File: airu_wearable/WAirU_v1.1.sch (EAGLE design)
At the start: 57 parts, among them J2 2p-2.0, Q2 MMBT3904LT1G, Q3 MMBT3904LT1G, Q4 BSS84, Q6 BSS84, U2 CN3065-DFN8, U3 HDC1080DMBT, U4 CJT1117-3.3-SOT223, U6 PAM2401, U7 ESP32_WROOM32_SKINNY

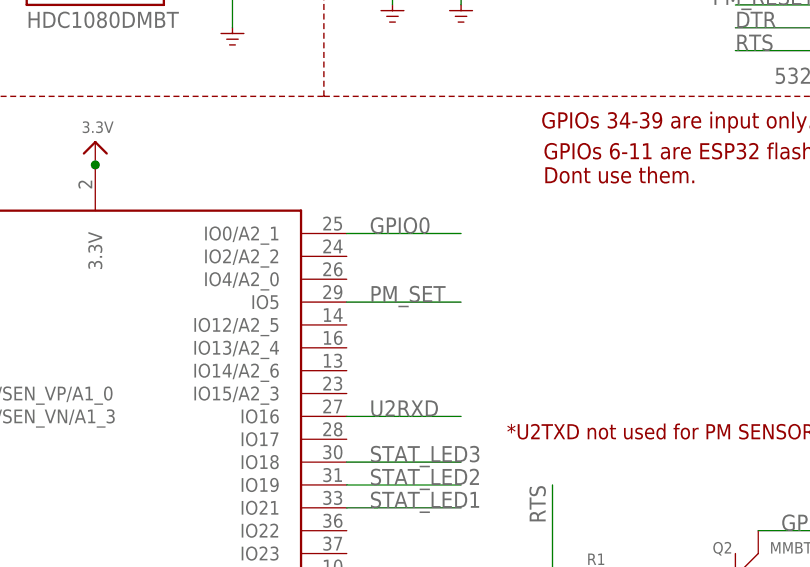
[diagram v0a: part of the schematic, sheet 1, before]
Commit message: changed PM_SET to GPIO4
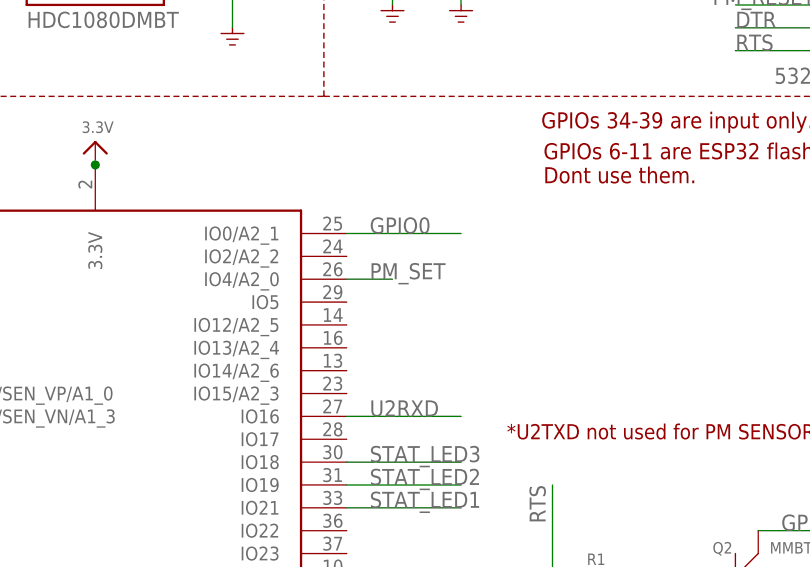
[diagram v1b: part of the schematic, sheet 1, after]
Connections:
- net PM_SET: now also U7.IO4/A2_0; no longer U7.IO5
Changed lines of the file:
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@@
 <net name="PM_SET" class="0">
-<segment>
-<pinref part="U7" gate="G$1" pin="IO5"/>
-<wire x1="78.74" y1="109.22" x2="91.44" y2="109.22" width="0.1524" layer="91"/>
-<label x="81.28" y="109.22" size="1.778" layer="95"/>
-</segment>
 <segment>
 <wire x1="121.92" y1="149.86" x2="134.62" y2="149.86" width="0.1524" layer="91"/>
@@
 <pinref part="U7" gate="G$1" pin="RXD0"/>
 </segment>
+<segment>
+<pinref part="U7" gate="G$1" pin="IO4/A2_0"/>
+<wire x1="78.74" y1="111.76" x2="83.82" y2="111.76" width="0.1524" layer="91"/>
+<label x="81.28" y="111.76" size="1.778" layer="95"/>
+</segment>
 </net>

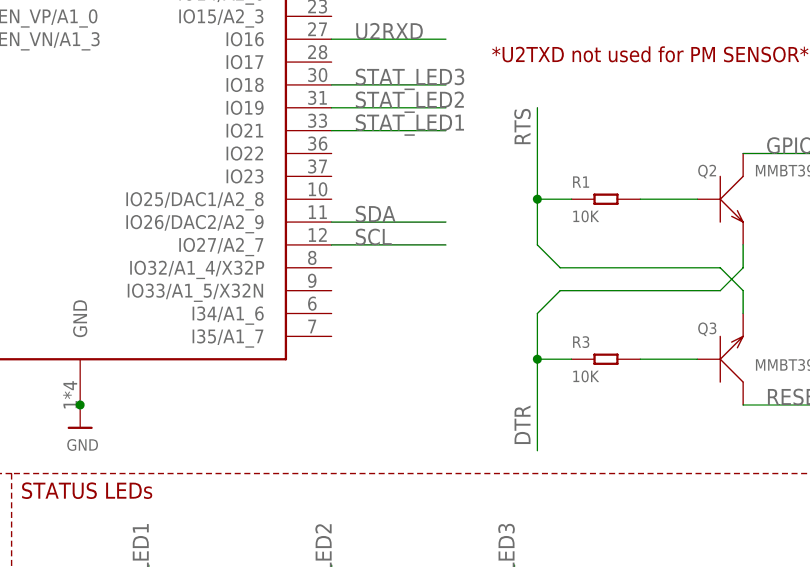
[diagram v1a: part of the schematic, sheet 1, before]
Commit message: routed PM_RESET and added dimensions, removed GND polygon from upper left
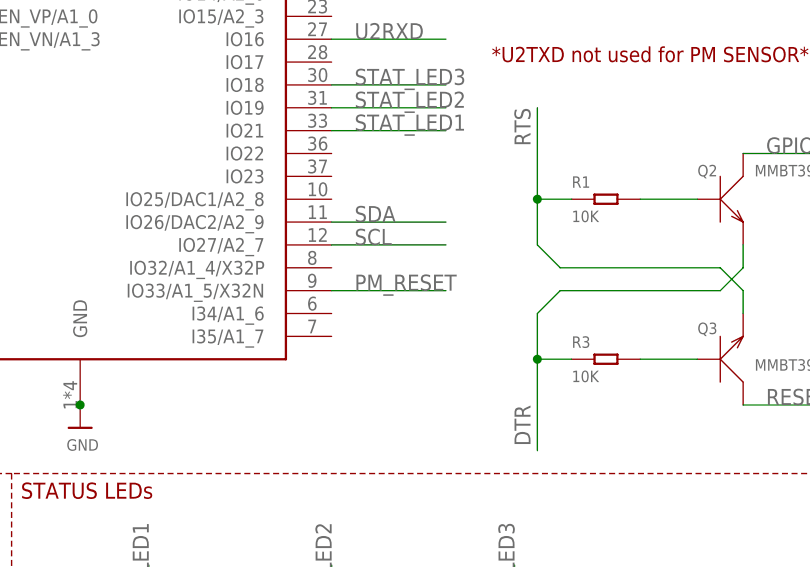
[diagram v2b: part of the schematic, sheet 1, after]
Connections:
- net PM_RESET: now also U7.IO33/A1_5/X32N
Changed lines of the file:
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@@
 <label x="119.38" y="142.24" size="1.778" layer="95"/>
+</segment>
+<segment>
+<pinref part="U7" gate="G$1" pin="IO33/A1_5/X32N"/>
+<wire x1="78.74" y1="68.58" x2="91.44" y2="68.58" width="0.1524" layer="91"/>
+<label x="81.28" y="68.58" size="1.778" layer="95"/>
 </segment>
 </net>

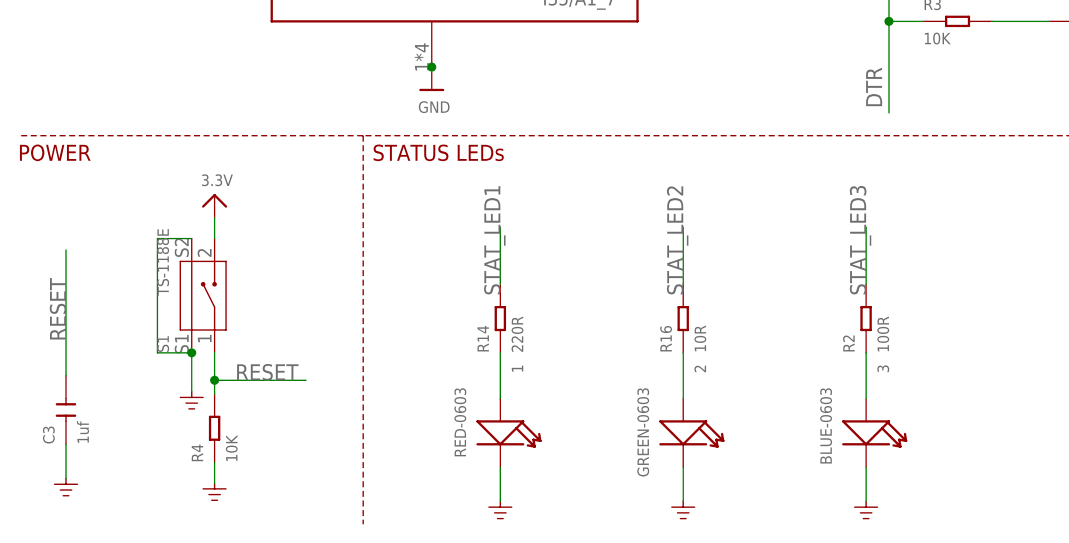
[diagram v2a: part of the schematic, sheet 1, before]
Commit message: - Remove led - Re-position Status Led 1 near the button - Replace reset button with SMD one - Route GND signal to ground plan - Add heat dissipation surrounding the temperature sensor - Remove ground plane copper pour from temperature sensor - Adjust board dimension, mounting holes dimention and position
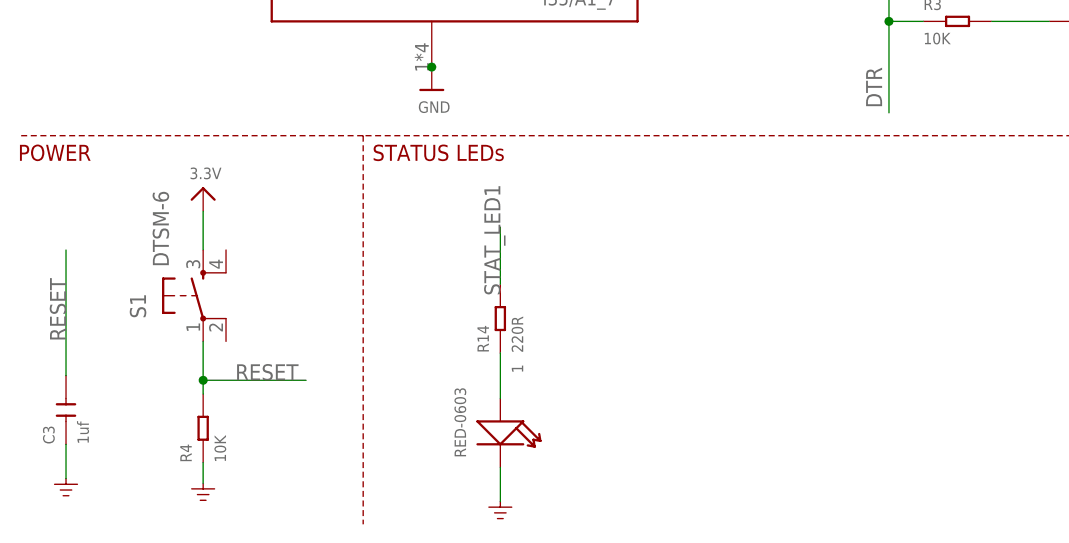
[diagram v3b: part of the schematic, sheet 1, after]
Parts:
- removed 2: GREEN-0603, Seeed-LED:SMD-LED-CLEAR-GREEN(0603)
- removed 3: BLUE-0603, Seeed-LED:SMD-LED-CLEAR-BLUE(0603)
- removed R16: 10R, Seeed-Resistor:SMD-RES-10R-5%-1/10W(0603)
- removed R2: 100R, Seeed-Resistor:SMD-RES-100R-5%-1/10W(0603)
- S1: value TS-1188E -> DTSM-6; device OPL_Switch:SMD-BUTTON(2+2P-7X3.5MM-90D) -> switch-tact:DTSM-6
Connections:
- removed net N$1: 2.+, R16.1
- removed net N$22: 3.+, R2.1
- net 3.3V: now also S1.3; no longer S1.2
- net GND: no longer 2.-, 3.-, S1.S1, S1.S2
- net STAT_LED2: no longer R16.2
- net STAT_LED3: no longer R2.2
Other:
- moved on the sheet: R4

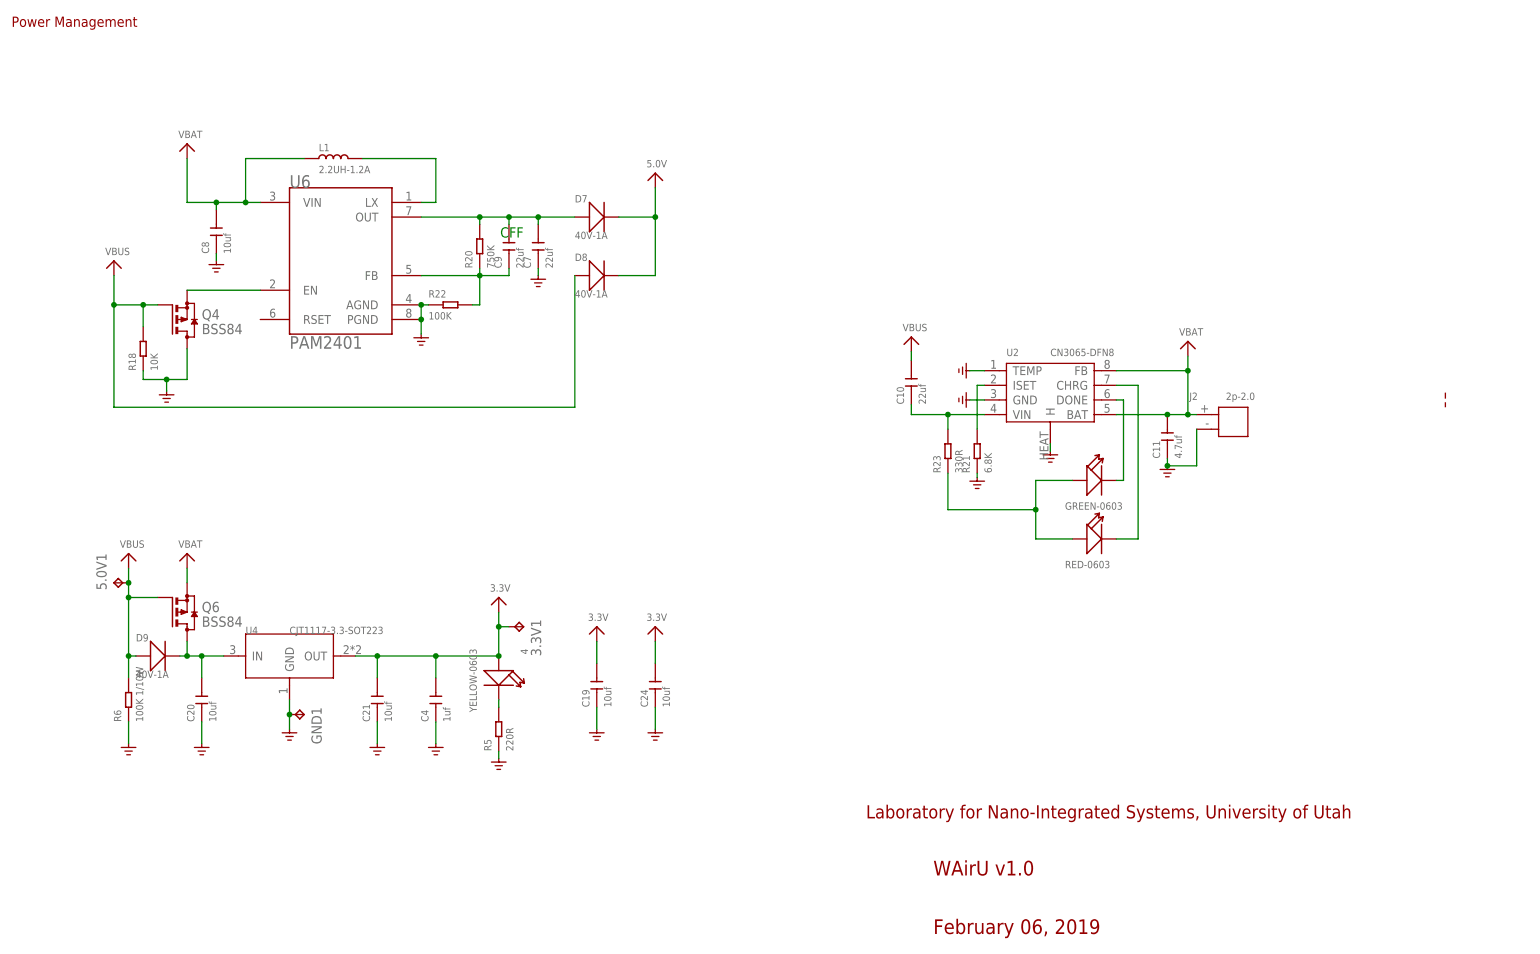
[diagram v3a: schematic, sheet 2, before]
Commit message: Change regulator, add rules for pads and vias, update new component to BOM sheet
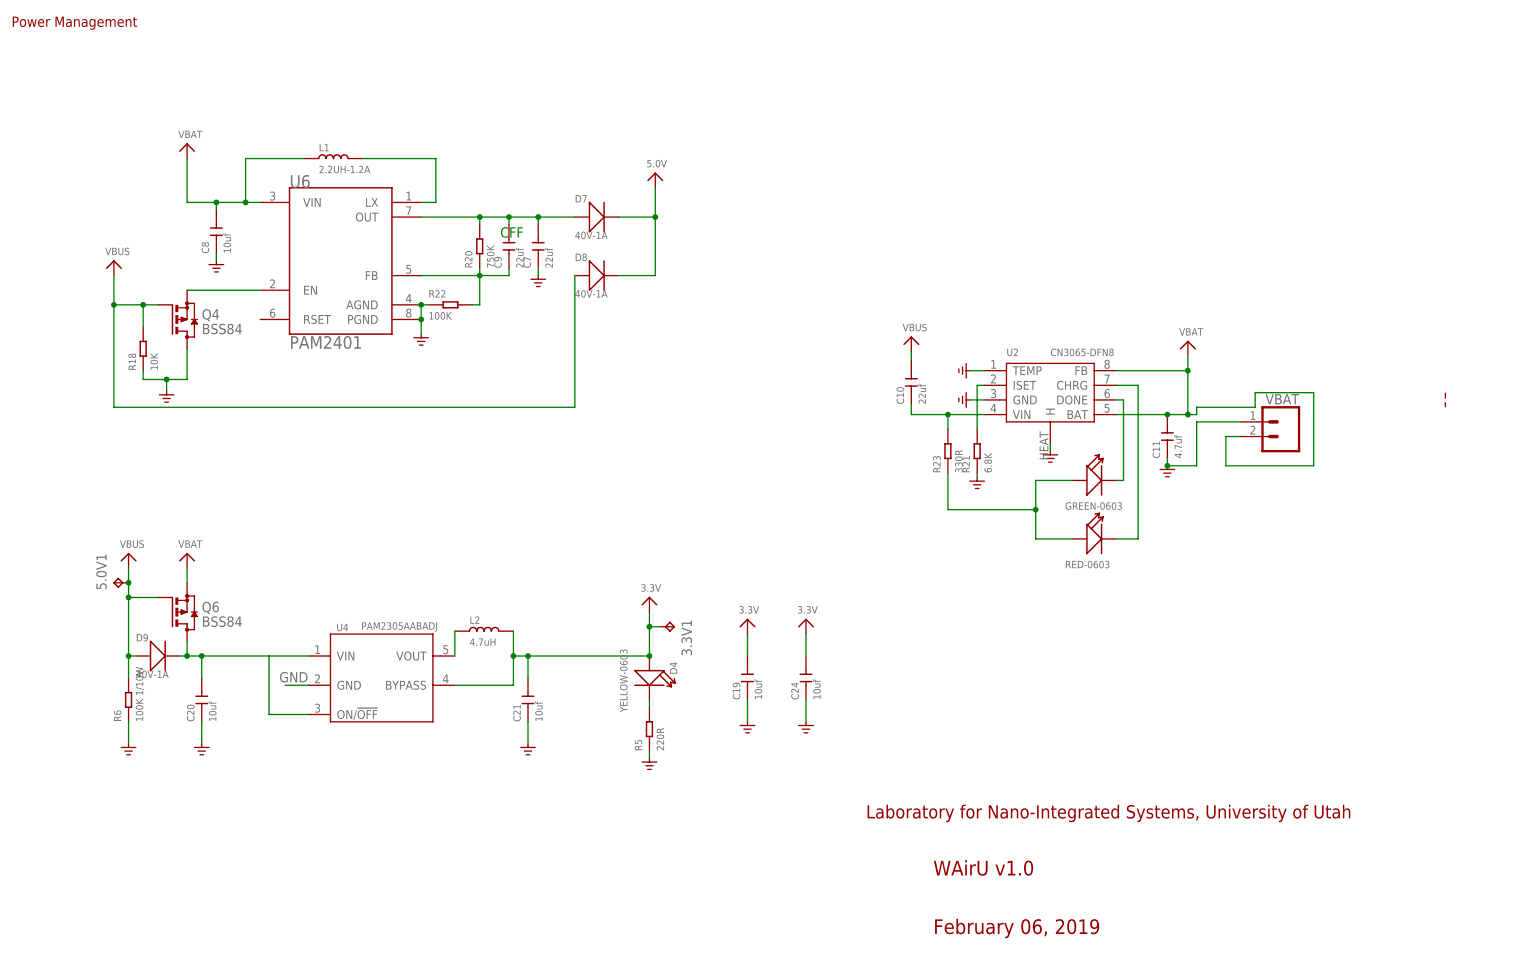
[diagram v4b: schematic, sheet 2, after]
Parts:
- removed 1: RED-0603, Seeed-LED:LED-SMD-RED-DIFFUSED(0603)
- removed 4: YELLOW-0603, Seeed-LED:SMD-LED-CLEAR-YELLOW(0603)
- removed C4: 1uf, Seeed-Capacitor:CERAMIC-1UF-25V-10%-X7R(0603)
- removed GND1: TPTP20SQ, testpad:TPTP20SQ
- removed J2: 2p-2.0, Seeed-Connector:DIP-JST-2P-2.0
- removed S1: DTSM-6, switch-tact:DTSM-6
- added D1: RED-0603, Seeed-LED:LED-SMD-RED-DIFFUSED(0603)
- added D4: YELLOW-0603, Seeed-LED:SMD-LED-CLEAR-YELLOW(0603)
- added K1: (no value), OPL_Switch:SMD-SWITCH-TACTILE-SPST-NO(4P-D6.0MM)
- added L2: 4.7uH, OPL_Inductor:SMD-INDUCTOR-10UH-20%-2.35A(2P-5X5X4MM)
- added VBAT: (no value), SparkFun-Connectors:CONN_02-JST-2MM-SMT
- U4: value CJT1117-3.3-SOT223 -> PAM2305AABADJ; device Seeed-IC:PMIC-CJT1117-3.3(SOT223) -> OPL_IC:PMIC-LP2985-33DBVR(SOT23-5)
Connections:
- new net N$75: C20.2, D9.-, Q6.D, U4.ON/!OFF, U4.VIN
- net 3.3V: now also D4.+, K1.B0, L2.2, U4.BYPASS; no longer 4.+, C4.2, S1.3, U4.OUT
- net GND: now also D1.-, VBAT.2; no longer 1.-, C4.1, GND1.TP, J2.P$2
- net N$21: now also D4.-; no longer 4.-
- net N$7: now also D1.+; no longer 1.+
- net N$8: now also L2.1, U4.VOUT; no longer C20.2, D9.-, Q6.D, U4.IN
- net RESET: now also K1.B1; no longer S1.1
- net VBAT: now also VBAT.1; no longer J2.P$1
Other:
- moved on the sheet: 3.3V1, C19, C21, C24, R5

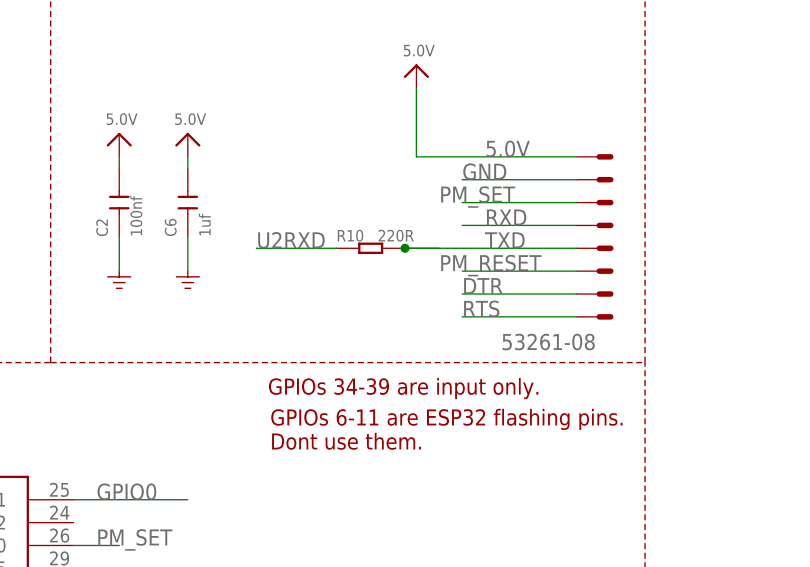
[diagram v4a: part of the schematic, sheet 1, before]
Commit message: Pull down PM_SET and PM_RESET
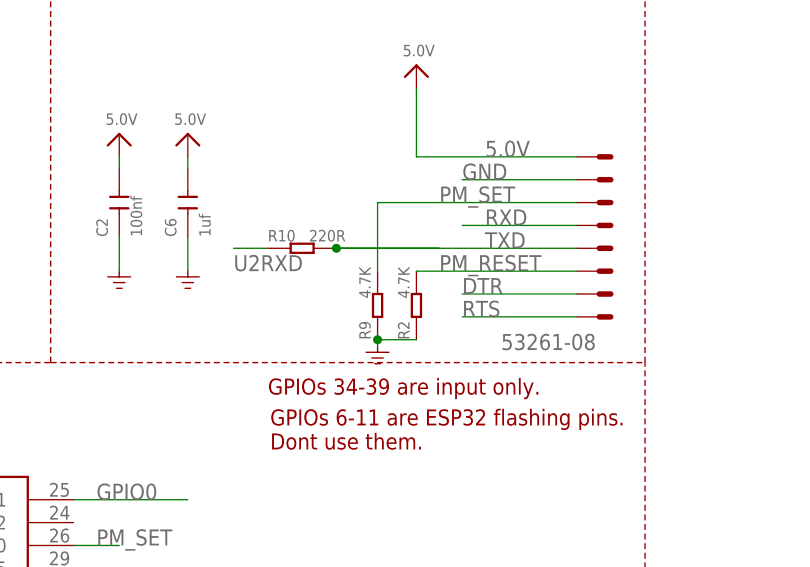
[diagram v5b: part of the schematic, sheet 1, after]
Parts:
- added R2, R9: 4.7K, Seeed-Resistor:SMD-RES-220R-5%-1/10W(0603)
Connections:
- net GND: now also R2.1, R9.1
- net PM_RESET: now also R2.2
- net PM_SET: now also R9.2
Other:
- moved on the sheet: R10
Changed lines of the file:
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@@
 <part name="K1" library="OPL_Switch" deviceset="SMD-SWITCH-TACTILE-SPST-NO(4P-D6.0MM)" device="" package3d_urn="urn:adsk.eagle:package:8005114/1"/>
 <part name="L2" library="OPL_Inductor" deviceset="SMD-INDUCTOR-10UH-20%-2.35A(2P-5X5X4MM)" device="" package3d_urn="urn:adsk.eagle:package:8004735/1" value="4.7uH"/>
+<part name="U$3" library="Power or GND " deviceset="GND_POWER" device=""/>
+<part name="R9" library="Seeed-Resistor" deviceset="SMD-RES-220R-5%-1/10W(0603)" device="" value="4.7K"/>
+<part name="R2" library="Seeed-Resistor" deviceset="SMD-RES-220R-5%-1/10W(0603)" device="" value="4.7K"/>
 </parts>
 <sheets>
@@
 <attribute name="VALUE" x="115.316" y="166.116" size="1.27" layer="96"/>
 </instance>
-<instance part="R10" gate="G$1" x="111.76" y="144.78" smashed="yes">
-<attribute name="NAME" x="107.95" y="145.542" size="1.27" layer="95" ratio="10"/>
-<attribute name="VALUE" x="112.522" y="145.542" size="1.27" layer="96" ratio="10"/>
+<instance part="R10" gate="G$1" x="104.14" y="144.78" smashed="yes">
+<attribute name="NAME" x="100.33" y="145.542" size="1.27" layer="95" ratio="10"/>
+<attribute name="VALUE" x="104.902" y="145.542" size="1.27" layer="96" ratio="10"/>
 </instance>
 <instance part="C2" gate="G$1" x="83.82" y="149.86" smashed="yes" rot="R90">
@@
 <attribute name="VALUE" x="21.59" y="36.576" size="1.27" layer="96" ratio="10" rot="R270"/>
 </instance>
+<instance part="U$3" gate="G$1" x="112.522" y="133.858" smashed="yes"/>
+<instance part="R9" gate="G$1" x="112.522" y="138.43" smashed="yes" rot="R90">
+<attribute name="NAME" x="111.76" y="134.62" size="1.27" layer="95" ratio="10" rot="R90"/>
+<attribute name="VALUE" x="111.76" y="139.192" size="1.27" layer="96" ratio="10" rot="R90"/>
+</instance>
+<instance part="R2" gate="G$1" x="116.84" y="138.43" smashed="yes" rot="R90">
+<attribute name="NAME" x="116.078" y="134.62" size="1.27" layer="95" ratio="10" rot="R90"/>
+<attribute name="VALUE" x="116.078" y="139.192" size="1.27" layer="96" ratio="10" rot="R90"/>
+</instance>
 </instances>
 <busses>
@@
 <wire x1="134.62" y1="152.4" x2="121.92" y2="152.4" width="0.1524" layer="91"/>
 <label x="121.92" y="152.4" size="1.778" layer="95"/>
+</segment>
+<segment>
+<pinref part="U$3" gate="G$1" pin="GND"/>
+<pinref part="R9" gate="G$1" pin="1"/>
+<wire x1="112.522" y1="133.858" x2="112.522" y2="134.62" width="0.1524" layer="91"/>
+<pinref part="R2" gate="G$1" pin="1"/>
+<wire x1="116.84" y1="134.62" x2="112.522" y2="134.62" width="0.1524" layer="91"/>
+<junction x="112.522" y="134.62"/>
 </segment>
 </net>
@@
 <segment>
 <pinref part="R10" gate="G$1" pin="1"/>
-<wire x1="107.95" y1="144.78" x2="99.06" y2="144.78" width="0.1524" layer="91"/>
-<label x="99.06" y="144.78" size="1.778" layer="95"/>
+<wire x1="100.33" y1="144.78" x2="96.52" y2="144.78" width="0.1524" layer="91"/>
+<label x="96.52" y="142.24" size="1.778" layer="95"/>
 </segment>
 </net>
@@
 <segment>
 <pinref part="MOLEX-53261-0871" gate="-3" pin="S"/>
-<wire x1="134.62" y1="142.24" x2="121.92" y2="142.24" width="0.1524" layer="91"/>
+<wire x1="134.62" y1="142.24" x2="116.84" y2="142.24" width="0.1524" layer="91"/>
 <label x="119.38" y="142.24" size="1.778" layer="95"/>
+<pinref part="R2" gate="G$1" pin="2"/>
 </segment>
 <segment>
@@
 <net name="PM_SET" class="0">
 <segment>
-<wire x1="121.92" y1="149.86" x2="134.62" y2="149.86" width="0.1524" layer="91"/>
 <pinref part="MOLEX-53261-0871" gate="-6" pin="S"/>
 <label x="119.38" y="149.86" size="1.778" layer="95"/>
+<wire x1="112.522" y1="149.86" x2="134.62" y2="149.86" width="0.1524" layer="91"/>
+<pinref part="R9" gate="G$1" pin="2"/>
+<wire x1="112.522" y1="149.86" x2="112.522" y2="142.24" width="0.1524" layer="91"/>
 </segment>
 <segment>
@@
 <segment>
 <pinref part="R10" gate="G$1" pin="2"/>
-<wire x1="115.57" y1="144.78" x2="119.38" y2="144.78" width="0.1524" layer="91"/>
-<wire x1="115.57" y1="144.78" x2="134.62" y2="144.78" width="0.1524" layer="91"/>
-<junction x="115.57" y="144.78"/>
+<wire x1="107.95" y1="144.78" x2="119.38" y2="144.78" width="0.1524" layer="91"/>
+<wire x1="107.95" y1="144.78" x2="134.62" y2="144.78" width="0.1524" layer="91"/>
+<junction x="107.95" y="144.78"/>
 <pinref part="MOLEX-53261-0871" gate="-4" pin="S"/>
 <label x="124.46" y="144.78" size="1.778" layer="95"/>
